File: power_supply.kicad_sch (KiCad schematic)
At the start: 87 parts, among them IC1 TPS54561DPRT, Q1 BSS138APW, Q2 BSS138-7-F, U1 AP62301WU-7, U11 AP62301WU-7, U2 AP62301WU-7, U3 AP62301WU-7, U4 74LVC1G123DP,125, U4_1 SN74LVC1G123YZPR

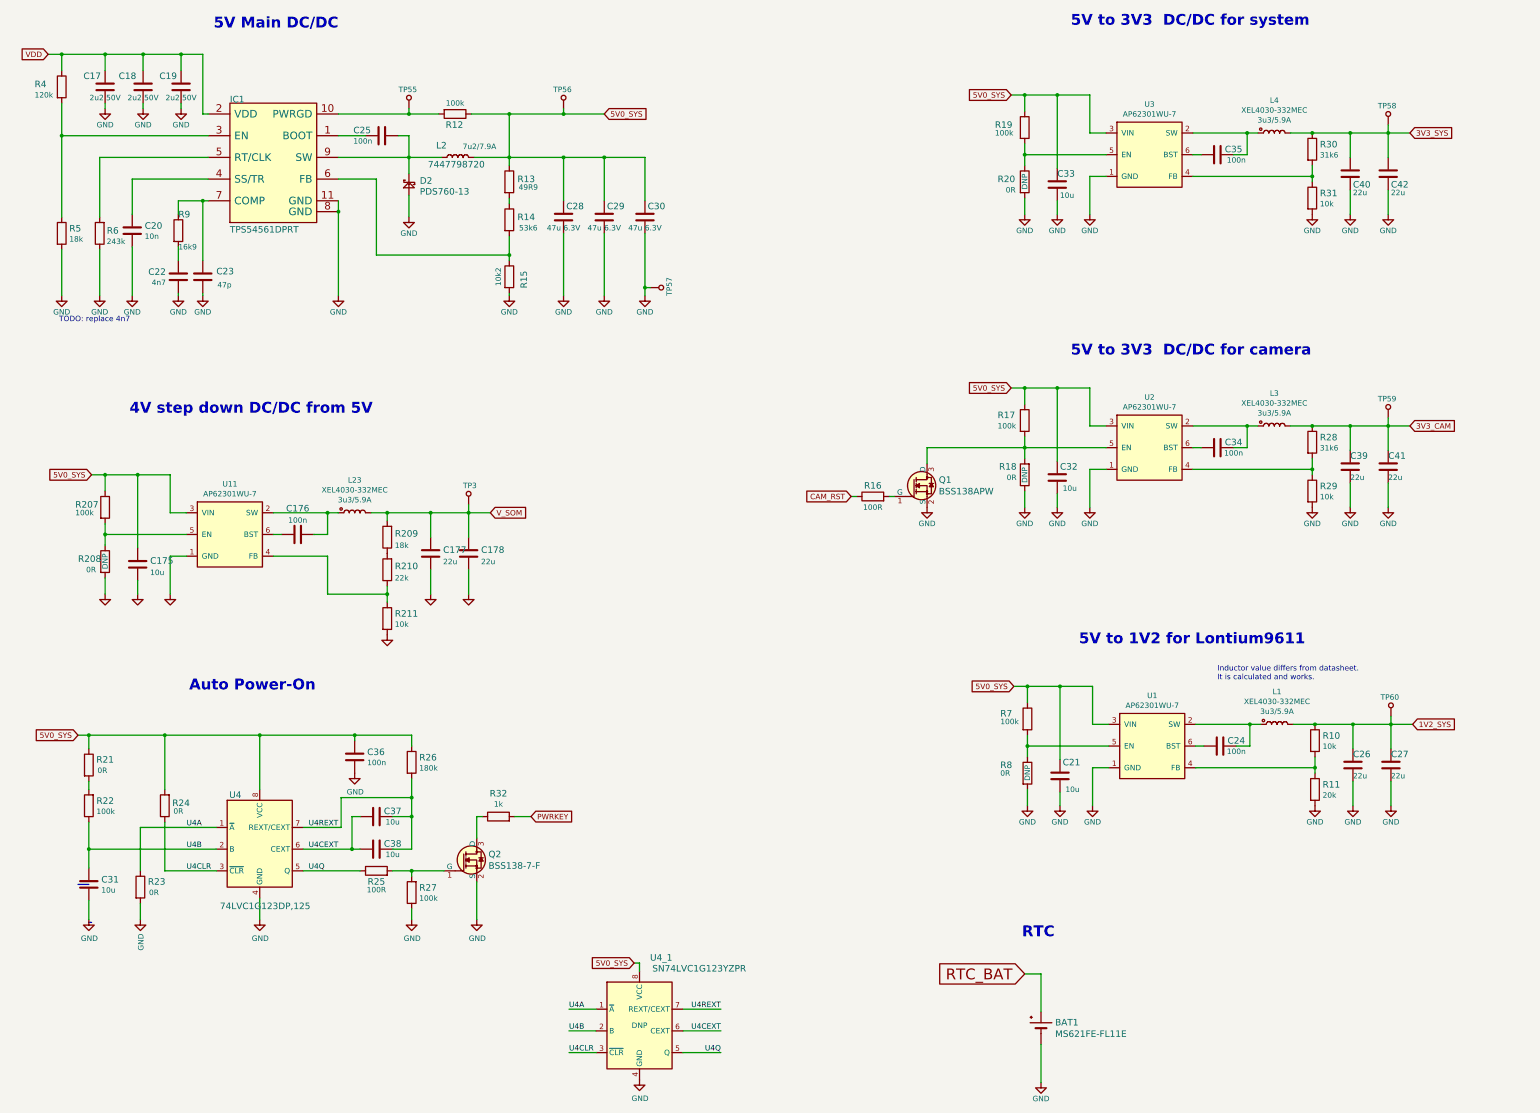
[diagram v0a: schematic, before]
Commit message: Cleared old files. Added 0R after DCDC converters
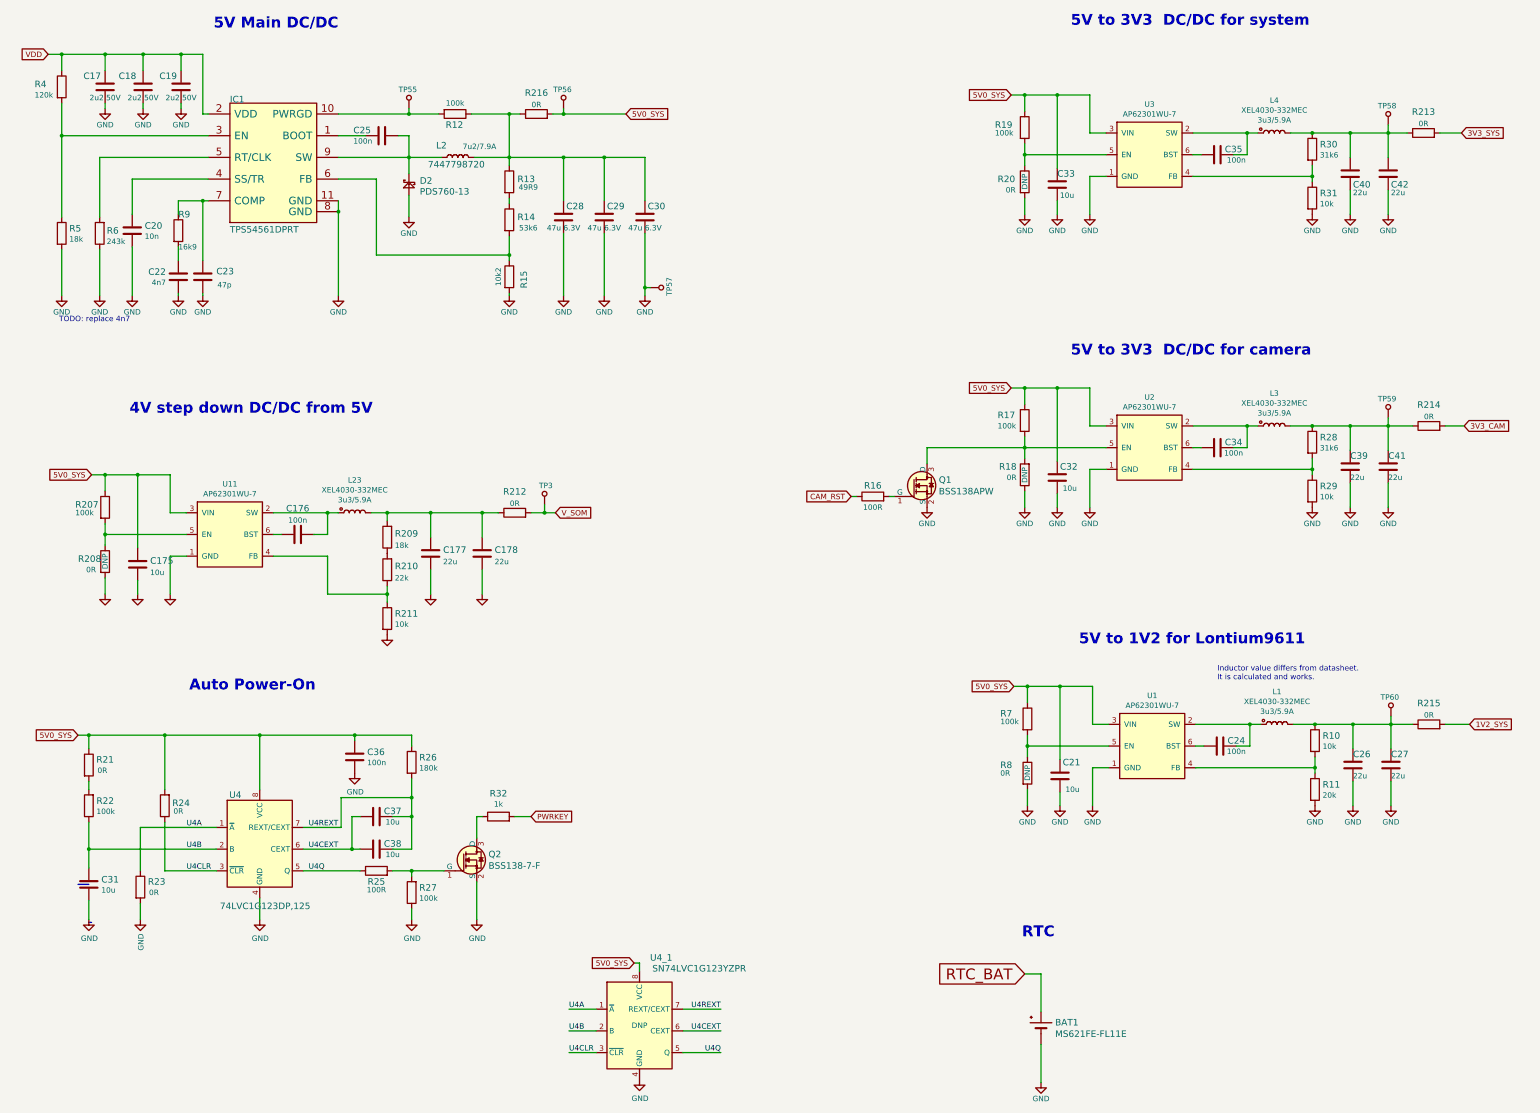
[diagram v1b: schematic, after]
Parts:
- added R212, R213, R214, R215, R216: R_0R_1206, antmicro-footprints:1206-res, symbol antmicroResistorsmisc:R_0R_1206
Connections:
- net 1V2_SYS: now also R215.2; no longer C26.1, C27.1, L1.2 (P), R10.1, TP60.1
- net 3V3_CAM: now also R214.2; no longer C39.1, C41.1, L3.2 (P), R28.1, TP59.1
- net 3V3_SYS: now also R213.2; no longer C40.1, C42.1, L4.2 (P), R30.1, TP58.1
- net 5V0_SYS: now also R216.2; no longer C28.1, C29.1, C30.1, L2.2 (P), R12.1, R13.1
- net V_SOM: now also R212.2; no longer C177.1, C178.1, L23.2 (P), R209.2
- new net: C40.1, C42.1, L4.2 (P), R213.1, R30.1, TP58.1
- new net: C39.1, C41.1, L3.2 (P), R214.1, R28.1, TP59.1
- new net: C26.1, C27.1, L1.2 (P), R10.1, R215.1, TP60.1
- new net: C28.1, C29.1, C30.1, L2.2 (P), R12.1, R13.1, R216.1
- new net: C177.1, C178.1, L23.2 (P), R209.2, R212.1
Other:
- moved on the sheet: C178, TP3

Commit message: Introduce component standardization
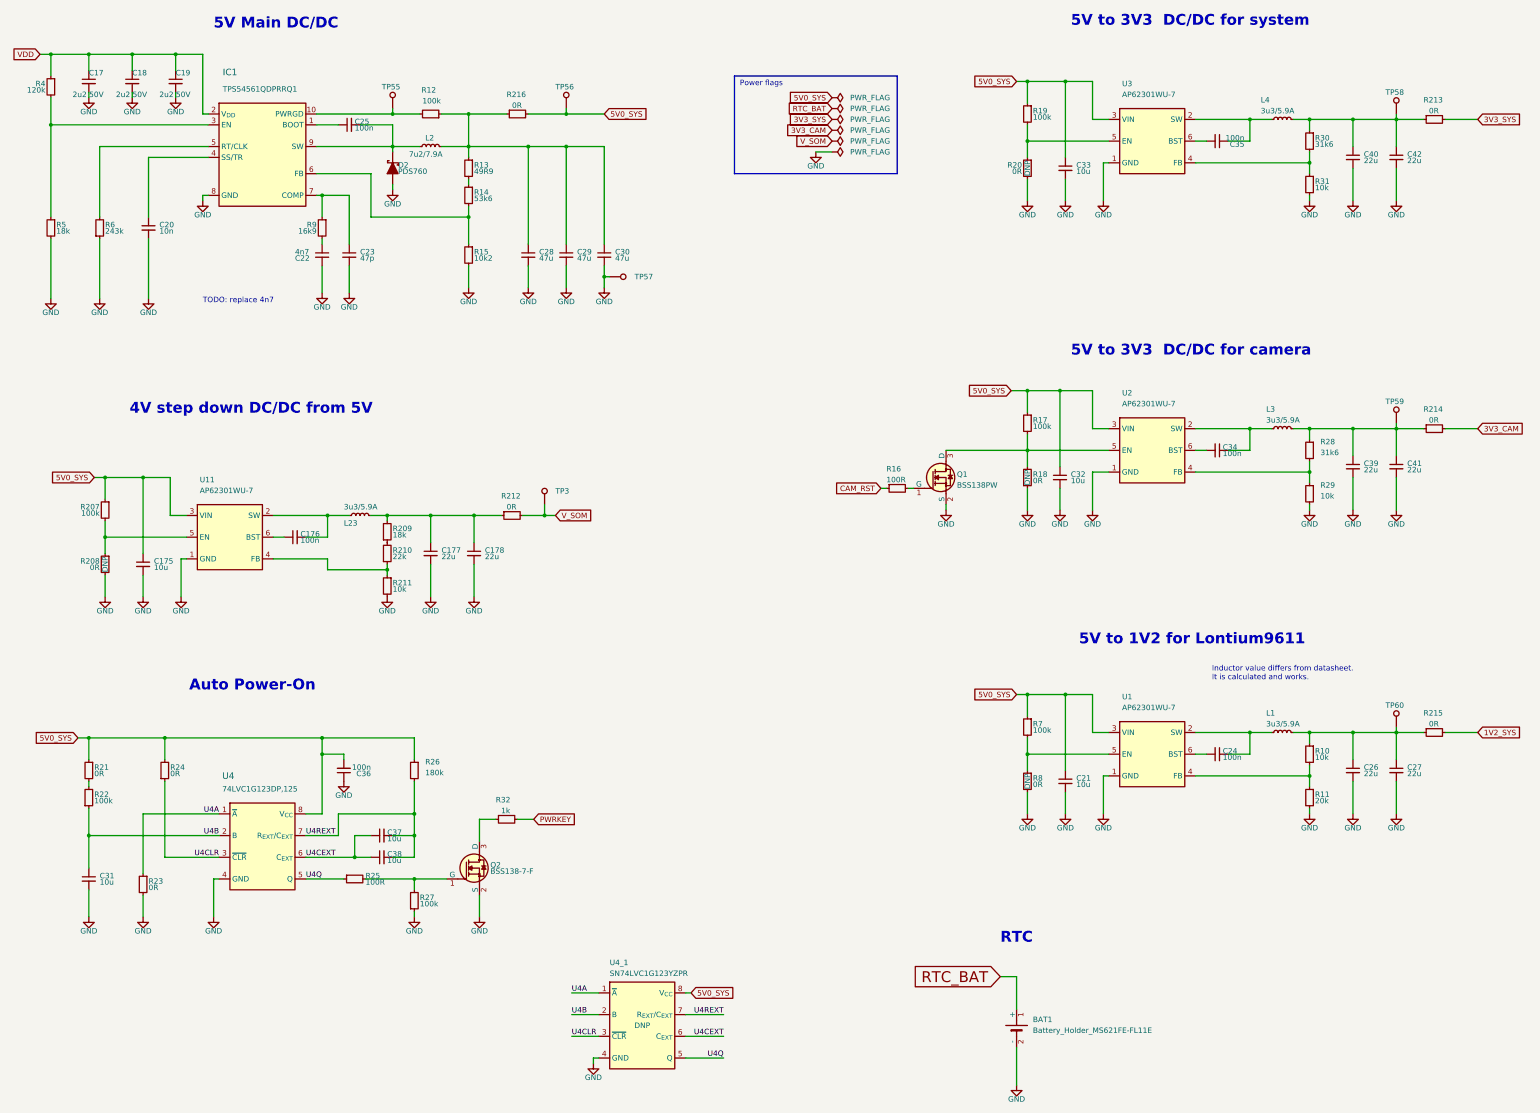
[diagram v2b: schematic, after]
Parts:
- BAT1: value MS621FE-FL11E -> Battery_Holder_MS621FE-FL11E; symbol sc606-baseboard:MS621FE-FL11E -> sc606-baseboard:Battery_Holder_MS621FE-FL11E; Author (none) -> Antmicro; License (none) -> Apache-2.0
- C17, C18, C19: footprint sc606-baseboard-footprints:0805-cap -> sc606-baseboard-footprints:C_0805_2012Metric; Author (none) -> Antmicro; License (none) -> Apache-2.0
- C175: footprint antmicro-footprints:0402-cap -> sc606-baseboard-footprints:C_0402_1005Metric; symbol antmicroCapacitors0402:C_10u_0402 -> sc606-baseboard:C_10u_0402; Author (none) -> Antmicro; License (none) -> Apache-2.0; Manufacturer YAGEO -> Yaego
- C176: footprint antmicro-footprints:0402-cap -> sc606-baseboard-footprints:C_0402_1005Metric; symbol antmicroCapacitors0402:C_100n_0402 -> sc606-baseboard:C_100n_0402; Author (none) -> Antmicro; Dielectric (none) -> X5R; License (none) -> Apache-2.0; Voltage (none) -> 50V
- C177, C178: footprint antmicro-footprints:0402-cap -> sc606-baseboard-footprints:C_0402_1005Metric; symbol antmicroCapacitors0402:C_22u_0402 -> sc606-baseboard:C_22u_0402; Author (none) -> Antmicro; License (none) -> Apache-2.0
- C20: footprint sc606-baseboard-footprints:0402-cap -> sc606-baseboard-footprints:C_0402_1005Metric; Author (none) -> Antmicro; Dielectric (none) -> X7R; License (none) -> Apache-2.0; MPN 04025G103ZAT2A -> GRM155R71H103KA88D; Manufacturer AVX -> Murata; Voltage (none) -> 50V
- C21, C31, C32, C33, C37, C38: footprint sc606-baseboard-footprints:0402-cap -> sc606-baseboard-footprints:C_0402_1005Metric; Author (none) -> Antmicro; License (none) -> Apache-2.0; Manufacturer YAGEO -> Yaego
- C22: footprint sc606-baseboard-footprints:0402-cap -> sc606-baseboard-footprints:C_0402_1005Metric; Author (none) -> Antmicro; License (none) -> Apache-2.0
- C23: footprint sc606-baseboard-footprints:0402-cap -> sc606-baseboard-footprints:C_0402_1005Metric; Author (none) -> Antmicro; Dielectric (none) -> C0G; License (none) -> Apache-2.0; MPN C0402C470J5GACTU -> GRM1555C1E470JA01D; Manufacturer KEMET -> Murata
- C24, C34, C35, C36: footprint sc606-baseboard-footprints:0402-cap -> sc606-baseboard-footprints:C_0402_1005Metric; Author (none) -> Antmicro; Dielectric (none) -> X5R; License (none) -> Apache-2.0; Voltage (none) -> 50V
- C25: footprint sc606-baseboard-footprints:0402-cap -> sc606-baseboard-footprints:C_0402_1005Metric; Author (none) -> Antmicro; Dielectric (none) -> X5R; License (none) -> Apache-2.0; MPN 0402X104K6R3CT -> GRM155R61H104KE14D; Manufacturer Walsin -> Murata; Voltage (none) -> 50V
- C26, C27, C39, C40, C41, C42: footprint sc606-baseboard-footprints:0603-cap -> sc606-baseboard-footprints:C_0603_1608Metric; Author (none) -> Antmicro; License (none) -> Apache-2.0; Manufacturer MURATA -> Murata
- C28, C29, C30: footprint sc606-baseboard-footprints:0603-cap -> sc606-baseboard-footprints:C_0603_1608Metric; Author (none) -> Antmicro; License (none) -> Apache-2.0; Manufacturer MURATA -> Murata; Val 47u 6.3V -> 47u
- D2: value PDS760-13 -> PDS760; footprint sc606-baseboard-footprints:PDS760-13 -> sc606-baseboard-footprints:PowerDI5; symbol sc606-baseboard:PDS760-13 -> sc606-baseboard:PDS760; Author (none) -> Antmicro; License (none) -> Apache-2.0; Manufacturer Diodes Inc. -> Diodes Incorporated
- IC1: value TPS54561DPRT -> TPS54561QDPRRQ1; footprint sc606-baseboard-footprints:WSON-10_4x4 -> sc606-baseboard-footprints:WSON-10-1EP_4x4mm_P0.8mm_EP2.6x3mm; symbol sc606-baseboard:TPS54561DPRT -> sc606-baseboard:TPS54561QDPRRQ1; Author (none) -> Antmicro; License (none) -> Apache-2.0; MPN TPS54561DPRT -> TPS54561QDPRRQ1; Manufacturer Texas Instrumets -> Texas Instruments
- L1, L23, L3, L4: value XEL4030-332MEC -> L_3u3_5.9A_XEL4030; footprint sc606-baseboard-footprints:Coilcraft-XEL4030 -> sc606-baseboard-footprints:L_Coilcraft_XEL4030; symbol sc606-baseboard:XEL4030-332MEC -> sc606-baseboard:L_3u3_5.9A_XEL4030; Author (none) -> Antmicro; License (none) -> Apache-2.0; MaxCur 5.9A -> (none)
- L2: value 7447798720 -> L_7u2_7.9A_WE-PDF; footprint sc606-baseboard-footprints:WE_7447798720 -> sc606-baseboard-footprints:L_WE-PDF; symbol sc606-baseboard:7447798720 -> sc606-baseboard:L_7u2_7.9A_WE-PDF; Author (none) -> Antmicro; License (none) -> Apache-2.0; Manufacturer Wurth Elektronik -> Würth Elektronik; MaxCur 7.9A -> (none)
- Q1: value BSS138APW -> BSS138PW; symbol sc606-baseboard:BSS138APW -> sc606-baseboard:BSS138PW; Author (none) -> Antmicro; License (none) -> Apache-2.0; Manufacturer ON Semiconductor -> Nexperia
- Q2: Author (none) -> Antmicro; License (none) -> Apache-2.0
- R10, R211, R29, R31: footprint sc606-baseboard-footprints:0402-res -> sc606-baseboard-footprints:R_0402_1005Metric; Author (none) -> Antmicro; License (none) -> Apache-2.0; MPN CRCW040210K0FKEDHP -> CR0402-FX-1002GLF; Manufacturer VISHAY -> Bourns; Tolerance (none) -> 1%
- R11: footprint sc606-baseboard-footprints:0402-res -> sc606-baseboard-footprints:R_0402_1005Metric; Author (none) -> Antmicro; License (none) -> Apache-2.0; MPN CRCW040220K0FKED -> CR0402-FX-2002GLF; Manufacturer VISHAY -> Bourns; Tolerance (none) -> 1%
- R12, R17, R19, R22, R27, R7: footprint sc606-baseboard-footprints:0402-res -> sc606-baseboard-footprints:R_0402_1005Metric; Author (none) -> Antmicro; License (none) -> Apache-2.0; MPN CRCW0402100KFKEDHP -> CR0402-FX-1003GLF; Manufacturer VISHAY -> Bourns; Tolerance (none) -> 1%
- R13: footprint sc606-baseboard-footprints:0603-res -> sc606-baseboard-footprints:R_0603_1608Metric; Author (none) -> Antmicro; License (none) -> Apache-2.0; MPN CRCW060349R9FKEA -> CR0603-FX-49R9ELF; Manufacturer Vishay -> Bourns; Tolerance (none) -> 1%
- R14: footprint sc606-baseboard-footprints:0402-res -> sc606-baseboard-footprints:R_0402_1005Metric; Author (none) -> Antmicro; License (none) -> Apache-2.0; MPN CPF0402B53K6E1 -> CR0402-FX-5362GLF; Manufacturer TE_CONNECTIVITY -> Bourns; Tolerance (none) -> 1%
- R15: footprint sc606-baseboard-footprints:0402-res -> sc606-baseboard-footprints:R_0402_1005Metric; Author (none) -> Antmicro; License (none) -> Apache-2.0; MPN MCWR04X1022FTL -> CR0402-FX-1022GLF; Manufacturer MULTICOMP -> Bourns; Tolerance (none) -> 1%
- R16, R25, R32: footprint sc606-baseboard-footprints:0402-res -> sc606-baseboard-footprints:R_0402_1005Metric; Author (none) -> Antmicro; License (none) -> Apache-2.0; Manufacturer BOURNS -> Bourns; Tolerance (none) -> 1%
- R18, R20, R21, R23, R24, R8: footprint sc606-baseboard-footprints:0402-res -> sc606-baseboard-footprints:R_0402_1005Metric; Author (none) -> Antmicro; Current (none) -> 1A; License (none) -> Apache-2.0; Manufacturer PANASONIC -> Panasonic
- R207: value ~ -> R_100k_0402; footprint sc606-baseboard-footprints:0402-res -> sc606-baseboard-footprints:R_0402_1005Metric; Author (none) -> Antmicro; License (none) -> Apache-2.0; MPN CRCW0402100KFKEDHP -> CR0402-FX-1003GLF; Manufacturer VISHAY -> Bourns; Tolerance (none) -> 1%
- R208: value ~ -> R_0R_0402; footprint sc606-baseboard-footprints:0402-res -> sc606-baseboard-footprints:R_0402_1005Metric; Author (none) -> Antmicro; Current (none) -> 1A; License (none) -> Apache-2.0; Manufacturer PANASONIC -> Panasonic
- R209, R5: footprint sc606-baseboard-footprints:0402-res -> sc606-baseboard-footprints:R_0402_1005Metric; Author (none) -> Antmicro; License (none) -> Apache-2.0; MPN MCWR04X1802FTL -> CR0402-FX-1802GLF; Manufacturer MULTICOMP -> Bourns; Tolerance (none) -> 1%
- R210: footprint sc606-baseboard-footprints:0402-res -> sc606-baseboard-footprints:R_0402_1005Metric; Author (none) -> Antmicro; License (none) -> Apache-2.0; MPN ERJ-2RKF2202X -> CR0402-FX-2202GLF; Manufacturer Panasonic -> Bourns; Tolerance (none) -> 1%
- R212, R213, R214, R215, R216: footprint antmicro-footprints:1206-res -> sc606-baseboard-footprints:R_1206_3216Metric; symbol antmicroResistorsmisc:R_0R_1206 -> sc606-baseboard:R_0R_1206; Author (none) -> Antmicro; Current (none) -> 2A; License (none) -> Apache-2.0; Manufacturer MULTICOMP -> Multicomp
- R26: footprint sc606-baseboard-footprints:0402-res -> sc606-baseboard-footprints:R_0402_1005Metric; Author (none) -> Antmicro; License (none) -> Apache-2.0; MPN CRCW0402180KJNED -> CR0402-FX-1803GLF; Manufacturer Vishay -> Bourns; Tolerance (none) -> 1%
- R28, R30: footprint sc606-baseboard-footprints:0402-res -> sc606-baseboard-footprints:R_0402_1005Metric; Author (none) -> Antmicro; License (none) -> Apache-2.0; MPN CRCW040231K6FKEDC -> CR0402-FX-3162GLF; Manufacturer Vishay -> Bourns; Tolerance (none) -> 1%
- R4: footprint sc606-baseboard-footprints:0402-res -> sc606-baseboard-footprints:R_0402_1005Metric; Author (none) -> Antmicro; License (none) -> Apache-2.0; MPN CRCW0402120KFKED -> CR0402-FX-1203GLF; Manufacturer VISHAY -> Bourns; Tolerance (none) -> 1%
- R6: footprint sc606-baseboard-footprints:0402-res -> sc606-baseboard-footprints:R_0402_1005Metric; Author (none) -> Antmicro; License (none) -> Apache-2.0; MPN MCMR04X2433FTL -> CR0402-FX-2433GLF; Manufacturer MULTICOMP -> Bourns; Tolerance (none) -> 1%
- R9: footprint sc606-baseboard-footprints:0402-res -> sc606-baseboard-footprints:R_0402_1005Metric; Author (none) -> Antmicro; License (none) -> Apache-2.0; MPN ERA2AEB1692X -> CR0402-FX-1692GLF; Manufacturer PANASONIC -> Bourns; Tolerance (none) -> 1%
- TP3, TP55, TP56, TP57, TP58, TP59, TP60: value TP_SMD_1_5MM -> TP_1.5mm_SMD; footprint sc606-baseboard-footprints:TP-R-1.5 -> sc606-baseboard-footprints:TP_SMD_1.5mm; symbol sc606-baseboard:TP_SMD_0_75MM -> sc606-baseboard:TP_1.5mm_SMD; Author (none) -> Antmicro; License (none) -> Apache-2.0
- U1, U11, U2, U3: footprint sc606-baseboard-footprints:TSOT23-6 -> sc606-baseboard-footprints:AP62301WU-7-TSOT23-6; Author (none) -> Antmicro; License (none) -> Apache-2.0
- U4: footprint sc606-baseboard-footprints:TSSOP-8_W3mm -> sc606-baseboard-footprints:TSSOP-8_3x3mm_P0.65mm; Author (none) -> Antmicro; License (none) -> Apache-2.0
- U4_1: footprint sc606-baseboard-footprints:DSBGA-8_1.91x0.91mm -> sc606-baseboard-footprints:Texas_DSBGA-8_1.9x0.9mm_2x4_P0.5mm; Author (none) -> Antmicro; License (none) -> Apache-2.0
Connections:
- net GND: now also BAT1.2 (-); no longer BAT1.-
- net RTC_BAT: now also BAT1.1 (+); no longer BAT1.+
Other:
- note added: "Power flags"
- moved on the sheet: BAT1, C17, C175, C176, C177, C178, C18, C19, C20, C21, C22, C23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
